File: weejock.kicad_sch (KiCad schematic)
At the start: 44 parts, among them J2 JST-PH2, K1 PG1350, K10 PG1350, K11 PG1350, K12 PG1350, K13 PG1350, K14 PG1350, K15 PG1350, K16 PG1350, K17 PG1350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

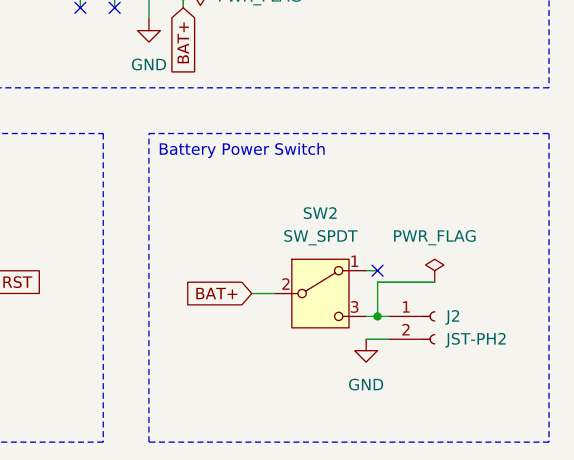
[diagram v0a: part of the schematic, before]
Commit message: Neatening power switch and adding ON/OFF labels.
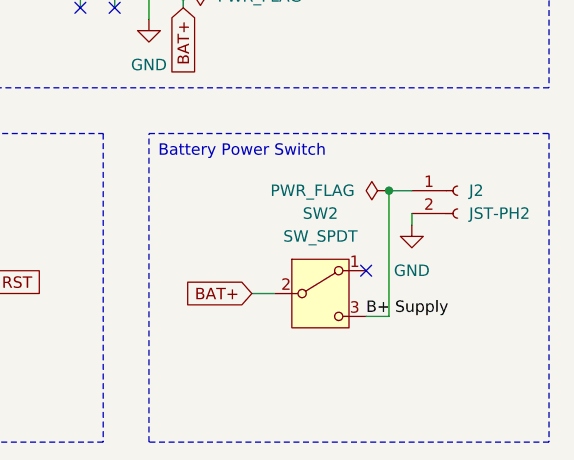
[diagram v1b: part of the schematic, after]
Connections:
- net B+ Supply: now reaches J2.1 (Pin_1), SW2.3 (C)
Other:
- moved on the sheet: J2
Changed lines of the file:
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@@
 	)
 	(junction
-		(at 82.55 54.61)
+		(at 185.42 93.98)
 		(diameter 0)
 		(color 0 0 0 0)
 	)
 	(junction
-		(at 57.15 81.28)
+		(at 82.55 54.61)
 		(diameter 0)
 		(color 0 0 0 0)
 	)
 	(junction
-		(at 184.15 107.95)
+		(at 57.15 81.28)
 		(diameter 0)
 		(color 0 0 0 0)
@@
 	)
 	(no_connect
-		(at 184.15 102.87)
-	)
-	(no_connect
 		(at 177.8 46.99)
 	)
@@
 	)
 	(no_connect
+		(at 182.88 102.87)
+	)
+	(no_connect
 		(at 154.94 26.67)
 	)
@@
 	(wire
 		(pts
-			(xy 190.5 104.14) (xy 184.15 104.14)
+			(xy 25.4 54.61) (xy 26.67 54.61)
 		)
 		(stroke
@@
 	(wire
 		(pts
-			(xy 25.4 54.61) (xy 26.67 54.61)
+			(xy 44.45 92.71) (xy 44.45 111.76)
 		)
 		(stroke
@@
 	(wire
 		(pts
-			(xy 44.45 92.71) (xy 44.45 111.76)
+			(xy 95.25 100.33) (xy 102.87 100.33)
 		)
 		(stroke
@@
 	(wire
 		(pts
-			(xy 95.25 100.33) (xy 102.87 100.33)
+			(xy 44.45 92.71) (xy 45.72 92.71)
 		)
 		(stroke
@@
 	(wire
 		(pts
-			(xy 44.45 92.71) (xy 45.72 92.71)
+			(xy 130.81 54.61) (xy 134.62 54.61)
 		)
 		(stroke
@@
 	(wire
 		(pts
-			(xy 130.81 54.61) (xy 134.62 54.61)
+			(xy 44.45 35.56) (xy 45.72 35.56)
 		)
 		(stroke
@@
 	(wire
 		(pts
-			(xy 44.45 35.56) (xy 45.72 35.56)
+			(xy 185.42 93.98) (xy 185.42 107.95)
 		)
 		(stroke
@@
 	(wire
 		(pts
-			(xy 182.88 107.95) (xy 184.15 107.95)
+			(xy 25.4 54.61) (xy 25.4 73.66)
 		)
 		(stroke
@@
 	(wire
 		(pts
-			(xy 25.4 54.61) (xy 25.4 73.66)
+			(xy 95.25 62.23) (xy 102.87 62.23)
 		)
 		(stroke
@@
 	(wire
 		(pts
-			(xy 95.25 62.23) (xy 102.87 62.23)
+			(xy 74.93 54.61) (xy 76.2 54.61)
 		)
 		(stroke
@@
 	(wire
 		(pts
-			(xy 74.93 54.61) (xy 76.2 54.61)
+			(xy 182.88 107.95) (xy 185.42 107.95)
 		)
 		(stroke
@@
 	(wire
 		(pts
-			(xy 95.25 119.38) (xy 102.87 119.38)
-		)
-		(stroke
-			(width 0)
-			(type default)
-		)
-	)
-	(wire
-		(pts
-			(xy 63.5 35.56) (xy 64.77 35.56)
+			(xy 187.96 97.79) (xy 187.96 96.52)
 		)
 		(stroke
@@
 	(wire
 		(pts
-			(xy 63.5 92.71) (xy 64.77 92.71)
+			(xy 95.25 119.38) (xy 102.87 119.38)
 		)
 		(stroke
@@
 	(wire
 		(pts
-			(xy 139.7 104.14) (xy 140.97 104.14)
+			(xy 63.5 35.56) (xy 64.77 35.56)
 		)
 		(stroke
@@
 	(wire
 		(pts
-			(xy 182.88 110.49) (xy 185.42 110.49)
+			(xy 63.5 92.71) (xy 64.77 92.71)
 		)
 		(stroke
@@
 	(wire
 		(pts
-			(xy 184.15 104.14) (xy 184.15 107.95)
+			(xy 139.7 104.14) (xy 140.97 104.14)
 		)
 		(stroke
@@
 	(wire
 		(pts
-			(xy 184.15 102.87) (xy 182.88 102.87)
-		)
-		(stroke
-			(width 0)
-			(type default)
-		)
-	)
-	(wire
-		(pts
 			(xy 63.5 73.66) (xy 63.5 92.71)
 		)
@@
 	(wire
 		(pts
+			(xy 185.42 93.98) (xy 187.96 93.98)
+		)
+		(stroke
+			(width 0)
+			(type default)
+		)
+	)
+	(wire
+		(pts
 			(xy 36.83 35.56) (xy 38.1 35.56)
 		)
@@
 	(wire
 		(pts
-			(xy 184.15 107.95) (xy 185.42 107.95)
-		)
-		(stroke
-			(width 0)
-			(type default)
-		)
-	)
-	(wire
-		(pts
 			(xy 130.81 50.8) (xy 134.62 50.8)
 		)
@@
 		)
 	)
+	(label "B+ Supply"
+		(at 182.88 107.95 0)
+		(effects
+			(font
+				(size 1.27 1.27)
+			)
+			(justify left bottom)
+		)
+	)
 	(global_label "RST"
 		(shape input)
@@
 	(symbol
 		(lib_id "weejock_keyboard_parts:JST-PH2")
-		(at 190.5 107.95 0)
+		(at 193.04 93.98 0)
 		(unit 1)
 		(exclude_from_sim no)
@@
 		(fields_autoplaced yes)
 		(property "Reference" "J2"
-			(at 191.77 107.9499 0)
+			(at 194.31 93.9799 0)
 			(effects
 				(font
@@
 		)
 		(property "Value" "JST-PH2"
-			(at 191.77 110.4899 0)
+			(at 194.31 96.5199 0)
 			(effects
 				(font
@@
 		)
 		(property "Footprint" "Connector_JST:JST_PH_S2B-PH-K_1x02_P2.00mm_Horizontal"
-			(at 190.5 107.95 0)
+			(at 193.04 93.98 0)
 			(effects
 				(font
@@
 		)
 		(property "Datasheet" "~"
-			(at 190.5 107.95 0)
+			(at 193.04 93.98 0)
 			(effects
 				(font
@@
 		)
 		(property "Description" "Generic connector, single row, 01x02, script generated"
-			(at 190.5 107.95 0)
+			(at 193.04 93.98 0)
 			(effects
 				(font
@@
 	(symbol
 		(lib_id "power:PWR_FLAG")
-		(at 190.5 104.14 0)
+		(at 185.42 93.98 90)
 		(unit 1)
 		(exclude_from_sim no)
@@
 		(fields_autoplaced yes)
 		(property "Reference" "#FLG01"
-			(at 190.5 102.235 0)
+			(at 183.515 93.98 0)
 			(effects
 				(font
@@
 		)
 		(property "Value" "PWR_FLAG"
-			(at 190.5 99.06 0)
+			(at 181.61 93.9799 90)
 			(effects
 				(font
 					(size 1.27 1.27)
 				)
+				(justify left)
 			)
 		)
 		(property "Footprint" ""
-			(at 190.5 104.14 0)
+			(at 185.42 93.98 0)
 			(effects
 				(font
@@
 		)
 		(property "Datasheet" "~"
-			(at 190.5 104.14 0)
+			(at 185.42 93.98 0)
 			(effects
 				(font
@@
 		)
 		(property "Description" "Special symbol for telling ERC where power comes from"
-			(at 190.5 104.14 0)
+			(at 185.42 93.98 0)
 			(effects
 				(font
@@
 	(symbol
 		(lib_id "power:GND")
-		(at 182.88 110.49 0)
+		(at 187.96 97.79 0)
 		(unit 1)
 		(exclude_from_sim no)
@@
 		(fields_autoplaced yes)
 		(property "Reference" "#PWR04"
-			(at 182.88 116.84 0)
+			(at 187.96 104.14 0)
 			(effects
 				(font
@@
 		)
 		(property "Value" "GND"
-			(at 182.88 115.57 0)
+			(at 187.96 102.87 0)
 			(effects
 				(font
@@
 		)
 		(property "Footprint" ""
-			(at 182.88 110.49 0)
+			(at 187.96 97.79 0)
 			(effects
 				(font
@@
 		)
 		(property "Datasheet" ""
-			(at 182.88 110.49 0)
+			(at 187.96 97.79 0)
 			(effects
 				(font
@@
 		)
 		(property "Description" "Power symbol creates a global label with name \"GND\" , ground"
-			(at 182.88 110.49 0)
+			(at 187.96 97.79 0)
 			(effects
 				(font
